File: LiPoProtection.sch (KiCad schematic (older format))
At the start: 51 parts, among them P1 CONN_01X05, P2 Load, P3 Supply, Q1 IRLML2502, U1 LM324, U2 LM324, U3 74HC08, U4 LP2950

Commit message: Added mass areas
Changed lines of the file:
@@
 $EndComp
 Wire Wire Line
-	6700 5350 6700 5950
-Wire Wire Line
-	6700 5950 6700 6700
+	6700 5350 6700 6700
 Wire Wire Line
 	8700 3725 9100 3725
@@
 	10100 3725 10000 3725
 Wire Wire Line
-	10000 3725 10000 3975
-Wire Wire Line
-	10000 3975 9700 3975
-Wire Wire Line
-	9700 3975 9400 3975
+	10000 3975 10000 3725
+Wire Wire Line
+	9400 3975 10000 3975
 Wire Wire Line
 	9400 3975 9400 3875
@@
 	2800 1050 3000 1050
 Wire Wire Line
-	2700 1550 2800 1550
-Wire Wire Line
-	2800 1550 2950 1550
+	2700 1550 2950 1550
 Wire Wire Line
 	2800 1350 2800 1550
@@
 	2100 1550 2400 1550
 Wire Wire Line
-	2100 1050 2100 1350
-Wire Wire Line
-	2100 1350 2100 1550
-Wire Wire Line
-	2100 1550 2100 2650
+	2100 1050 2100 2650
 Wire Wire Line
 	2000 1750 2400 1750
 Wire Wire Line
-	2000 1050 2000 1750
-Wire Wire Line
-	2000 1750 2000 7050
-Wire Wire Line
-	2700 1750 2800 1750
-Wire Wire Line
-	2800 1750 2950 1750
-Wire Wire Line
-	3950 1650 3950 2450
-Wire Wire Line
-	3950 2450 3950 2950
-Wire Wire Line
-	3500 2450 3600 2450
-Wire Wire Line
-	3600 2450 3950 2450
+	2000 1050 2000 7050
+Wire Wire Line
+	2700 1750 2950 1750
+Wire Wire Line
+	3950 1650 3950 2950
+Wire Wire Line
+	3500 2450 3950 2450
 Wire Wire Line
 	2800 2450 3200 2450
 Wire Wire Line
-	2800 1750 2800 2300
-Wire Wire Line
-	2800 2300 2800 2450
+	2800 1750 2800 2450
 Connection ~ 2800 1750
 Wire Wire Line
 	2550 1050 2300 1050
 Wire Wire Line
-	2550 600  2550 750
-Wire Wire Line
-	2550 750  2550 1050
-Wire Wire Line
-	2550 750  3350 750
-Wire Wire Line
-	3350 750  4575 750
-Wire Wire Line
-	4575 750  5400 750
-Wire Wire Line
-	5400 750  6350 750
-Wire Wire Line
-	6350 750  7600 750
+	2550 600  2550 1050
+Wire Wire Line
+	2550 750  7600 750
 Wire Wire Line
 	3350 750  3350 1250
@@
 	5400 2100 5400 2050
 Wire Wire Line
-	4750 1550 4850 1550
-Wire Wire Line
-	4850 1550 5000 1550
+	4750 1550 5000 1550
 Wire Wire Line
 	4850 1350 4850 1550
@@
 	4050 1750 4450 1750
 Wire Wire Line
-	4750 1750 4850 1750
-Wire Wire Line
-	4850 1750 5000 1750
-Wire Wire Line
-	6000 1650 6000 2450
-Wire Wire Line
-	6000 2450 6000 3100
-Wire Wire Line
-	5550 2450 5625 2450
-Wire Wire Line
-	5625 2450 6000 2450
+	4750 1750 5000 1750
+Wire Wire Line
+	6000 1650 6000 3100
+Wire Wire Line
+	5550 2450 6000 2450
 Wire Wire Line
 	4850 2450 5250 2450
 Wire Wire Line
-	4850 1750 4850 2300
-Wire Wire Line
-	4850 2300 4850 2450
+	4850 1750 4850 2450
 Connection ~ 4850 1750
 Wire Wire Line
@@
 	7600 2100 7600 2050
 Wire Wire Line
-	6950 1550 7050 1550
-Wire Wire Line
-	7050 1550 7200 1550
+	6950 1550 7200 1550
 Wire Wire Line
 	7050 1350 7050 1550
@@
 	6650 1750 6250 1750
 Wire Wire Line
-	6950 1750 7050 1750
-Wire Wire Line
-	7050 1750 7200 1750
-Wire Wire Line
-	8200 1650 8200 2450
-Wire Wire Line
-	8200 2450 8200 3250
-Wire Wire Line
-	7750 2450 8000 2450
-Wire Wire Line
-	8000 2450 8200 2450
+	6950 1750 7200 1750
+Wire Wire Line
+	8200 1650 8200 3250
+Wire Wire Line
+	7750 2450 8200 2450
 Wire Wire Line
 	7050 2450 7450 2450
 Wire Wire Line
-	7050 1750 7050 2325
-Wire Wire Line
-	7050 2325 7050 2450
+	7050 1750 7050 2450
 Connection ~ 7050 1750
 Wire Wire Line
@@
 	6250 2650 6250 1750
 Wire Wire Line
-	2200 1050 2200 1150
-Wire Wire Line
-	2200 1150 2200 1300
+	2200 1050 2200 1300
 Wire Wire Line
 	2200 1150 2650 1150
@@
 	2650 850  4150 850
 Wire Wire Line
-	4150 850  4150 1550
-Wire Wire Line
-	4150 1550 4150 2650
+	4150 850  4150 2650
 Connection ~ 4150 1550
 Wire Wire Line
@@
 Connection ~ 7600 750
 Wire Wire Line
-	4850 1050 4975 1050
-Wire Wire Line
-	4975 1050 5050 1050
+	4850 1050 5050 1050
 Wire Wire Line
 	7050 1050 7250 1050
@@
 	2000 7050 5550 7050
 Wire Wire Line
-	2300 1050 2300 1500
-Wire Wire Line
-	2300 1500 1725 1500
-Wire Wire Line
-	1725 1500 1150 1500
+	2300 1500 2300 1050
+Wire Wire Line
+	1150 1500 2300 1500
 Connection ~ 2300 1050
 Wire Wire Line
 	4100 6400 4100 6350
 Wire Wire Line
-	850  4250 875  4250
-Wire Wire Line
-	875  4250 1200 4250
-Wire Wire Line
-	1200 4250 1550 4250
+	850  4250 1550 4250
 Wire Wire Line
 	1150 1500 1150 1550
 Wire Wire Line
-	1150 1800 1150 2000
-Wire Wire Line
-	1150 2000 1150 2150
-Wire Wire Line
-	750  2000 1150 2000
-Wire Wire Line
-	1150 2000 1350 2000
+	1150 1800 1150 2150
+Wire Wire Line
+	750  2000 1350 2000
 Wire Wire Line
 	1350 2000 1350 4050
@@
 	1050 2750 1150 2750
 Wire Wire Line
-	1150 2550 1150 2750
-Wire Wire Line
-	1150 2750 1150 2850
-Wire Wire Line
-	750  2000 750  2350
-Wire Wire Line
-	750  2350 750  2750
+	1150 2550 1150 2850
+Wire Wire Line
+	750  2000 750  2750
 Wire Wire Line
 	750  2350 800  2350
@@
 	3700 6700 3950 6700
 Wire Wire Line
-	3700 6050 3700 6125
-Wire Wire Line
-	3700 6125 3700 6700
-Wire Wire Line
-	3500 6050 3550 6050
-Wire Wire Line
-	3550 6050 3700 6050
+	3700 6050 3700 6700
+Wire Wire Line
+	3500 6050 3700 6050
 Wire Wire Line
 	3550 6300 3550 6050
@@
 	5700 6700 5950 6700
 Wire Wire Line
-	5700 6050 5700 6125
-Wire Wire Line
-	5700 6125 5700 6700
-Wire Wire Line
-	5500 6050 5550 6050
-Wire Wire Line
-	5550 6050 5700 6050
+	5700 6050 5700 6700
+Wire Wire Line
+	5500 6050 5700 6050
 Wire Wire Line
 	5550 6300 5550 6050
@@
 	3700 5050 3950 5050
 Wire Wire Line
-	3700 4400 3700 4500
-Wire Wire Line
-	3700 4500 3700 5050
-Wire Wire Line
-	3500 4400 3550 4400
-Wire Wire Line
-	3550 4400 3700 4400
+	3700 4400 3700 5050
+Wire Wire Line
+	3500 4400 3700 4400
 Wire Wire Line
 	3550 4650 3550 4400
@@
 	5700 4950 5950 4950
 Wire Wire Line
-	5700 4300 5700 4375
-Wire Wire Line
-	5700 4375 5700 4950
-Wire Wire Line
-	5500 4300 5550 4300
-Wire Wire Line
-	5550 4300 5700 4300
+	5700 4300 5700 4950
+Wire Wire Line
+	5500 4300 5700 4300
 Wire Wire Line
 	5550 4550 5550 4300
@@
 	4700 6700 4250 6700
 Wire Wire Line
-	4700 5250 4700 5950
-Wire Wire Line
-	4700 5950 4700 6700
+	4700 5250 4700 6700
 Connection ~ 6700 5950
 Wire Wire Line
-	6700 4200 6700 4950
-Wire Wire Line
-	6700 4950 6700 5050
+	6700 4200 6700 5050
 Connection ~ 6700 4950
 Wire Wire Line
@@
 	4950 4850 4950 3250
 Wire Wire Line
-	4700 4300 4700 5050
-Wire Wire Line
-	4700 5050 4700 5150
+	4700 4300 4700 5150
 Connection ~ 4700 5050
 Connection ~ 4700 5950
@@
 	2950 4950 2950 3100
 Wire Wire Line
-	7650 3800 7650 4000
-Wire Wire Line
-	7650 4000 7650 4100
+	7650 3800 7650 4100
 Connection ~ 7650 4000
 Wire Wire Line
@@
 	1050 4775 1050 4625
 Wire Wire Line
-	875  4625 1050 4625
-Wire Wire Line
-	1050 4625 1200 4625
+	875  4625 1200 4625
 Connection ~ 1050 4625
 Wire Wire Line
@@
 	8700 4450 8700 3725
 Wire Wire Line
-	1050 600  1350 600
-Wire Wire Line
-	1350 600  2550 600
+	1050 600  2550 600
 Wire Wire Line
 	7950 4000 7650 4000
 Wire Wire Line
-	1725 1500 1725 5525
-Wire Wire Line
-	1725 5525 1725 5750
+	1725 1500 1725 5750
 Connection ~ 1725 1500
 Wire Wire Line
@@
 	1725 6050 1050 6050
 Wire Wire Line
-	1050 6050 1050 5900
-Wire Wire Line
-	1050 5900 925  5900
-Wire Wire Line
-	925  5900 900  5900
+	1050 5900 1050 6050
+Wire Wire Line
+	900  5900 1050 5900
 Wire Wire Line
 	925  5625 925  5900
@@
 	875  5425 925  5425
 Wire Wire Line
-	4700 5250 7100 5250
-Wire Wire Line
-	7100 5250 7525 5250
+	4700 5250 7525 5250
 Wire Wire Line
 	7525 5250 7525 5050
@@
 	7775 5150 7775 5250
 Wire Wire Line
-	6700 5050 7200 5050
-Wire Wire Line
-	7200 5050 7225 5050
+	6700 5050 7225 5050
 Wire Wire Line
 	7225 5050 7225 5750

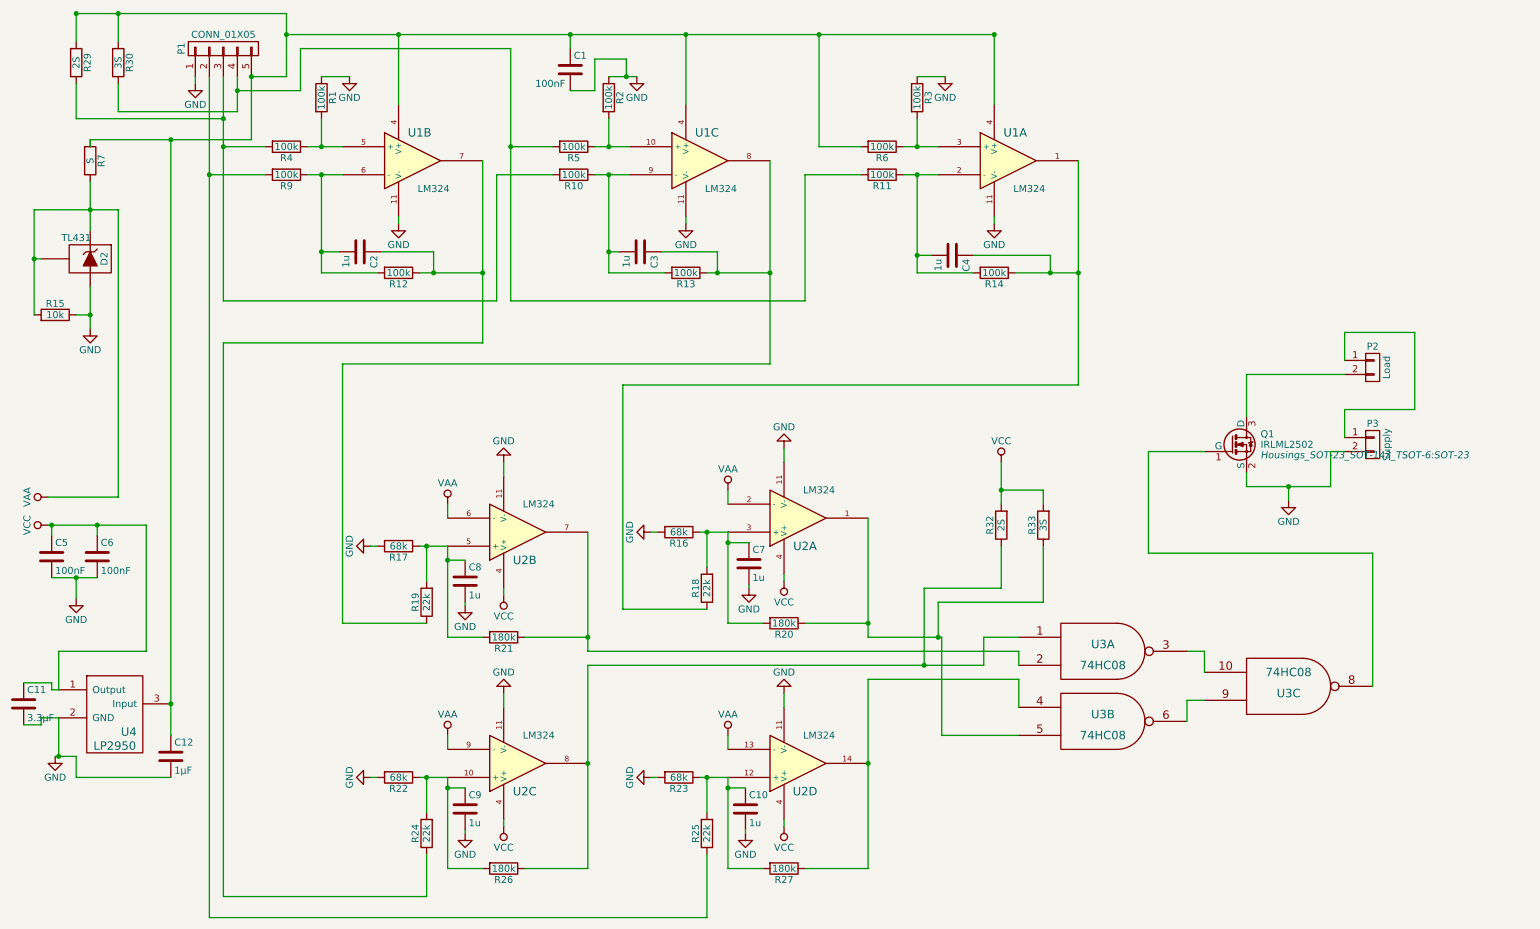
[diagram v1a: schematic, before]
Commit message: Added libraries, added flyout diode
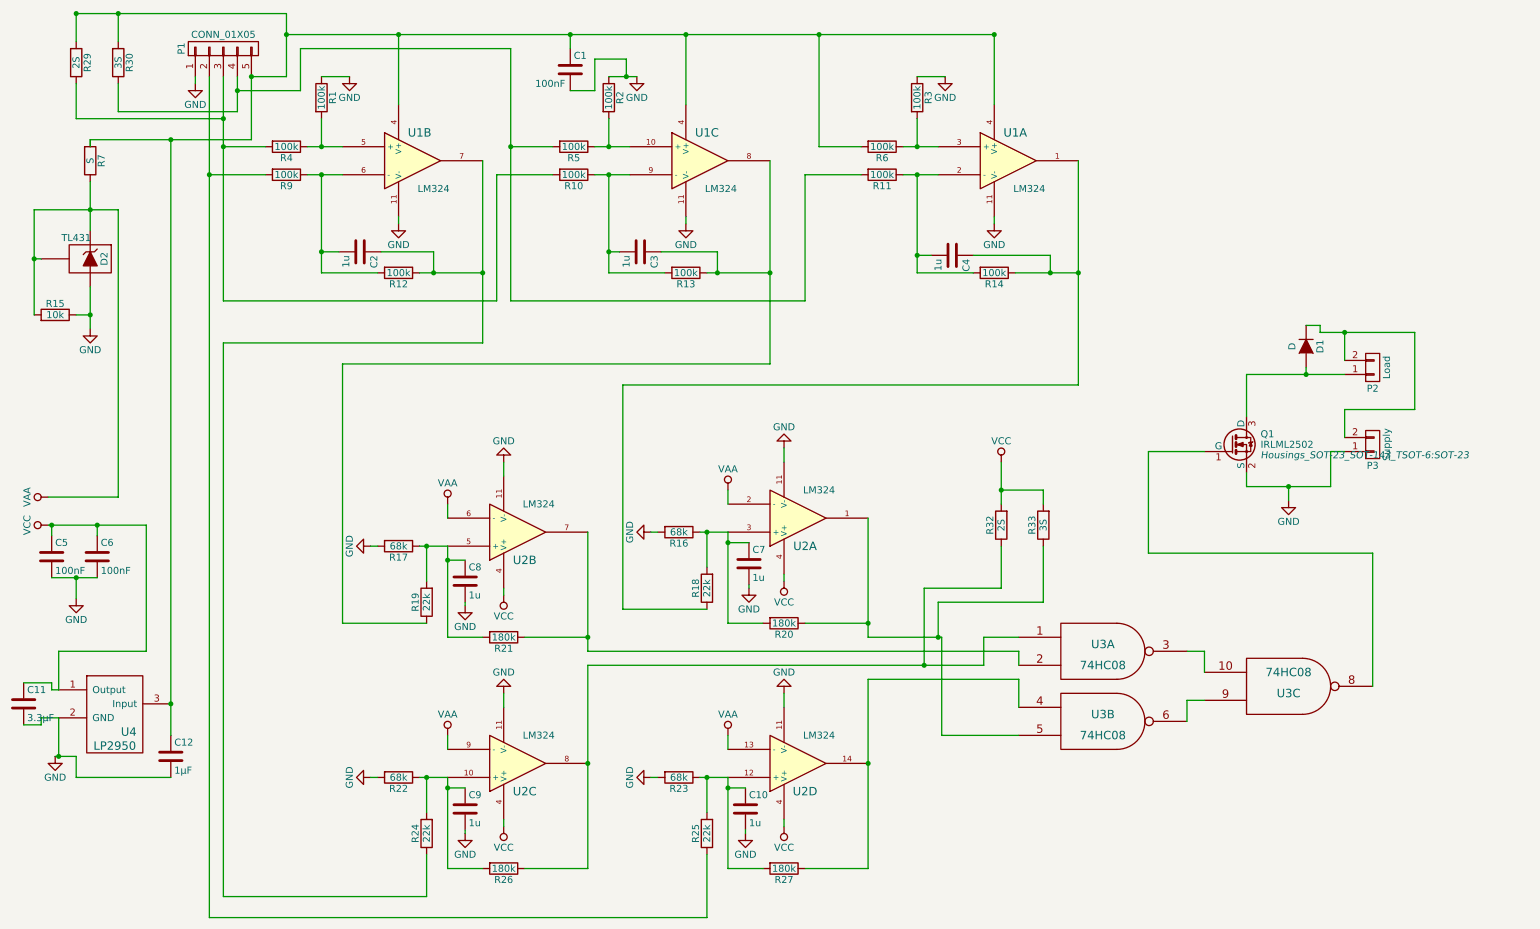
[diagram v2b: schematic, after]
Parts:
- added D1: D, Diodes_ThroughHole:Diode_DO-41_SOD81_Horizontal_RM10, symbol D
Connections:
- net GND: now also P3.1 (P1); no longer P3.2 (P2)
- net at Q1.3 (D): now also P2.1 (P1), D1.2 (A); no longer P2.2 (P2)
- new net: D1.1 (K), P2.2 (P2), P3.2 (P2)
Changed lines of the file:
@@
 LIBS:contrib
 LIBS:valves
-LIBS:cmos4000ex
+LIBS:74xx_ex
+LIBS:device_ex
+LIBS:regul_ex
 LIBS:transistors_ex
-LIBS:device_ex
-LIBS:74xx_ex
-LIBS:regul_ex
+LIBS:cmos4000_ex
 LIBS:LiPoProtection-cache
 EELAYER 25 0
@@
 F 3 "" H 10300 3675 60  0000 C CNN
 	1    10300 3675
-	1    0    0    -1
+	1    0    0    1
 $EndComp
 $Comp
@@
 F 3 "" H 10300 3125 60  0000 C CNN
 	1    10300 3125
-	1    0    0    -1
+	1    0    0    1
 $EndComp
 $Comp
@@
 	10100 3075 10100 2875
 Wire Wire Line
-	10100 2875 10600 2875
+	9925 2875 10600 2875
 Wire Wire Line
 	10600 2875 10600 3425
@@
 	10100 3725 10000 3725
 Wire Wire Line
-	10000 3975 10000 3725
-Wire Wire Line
-	9400 3975 10000 3975
+	10000 3725 10000 3975
+Wire Wire Line
+	10000 3975 9400 3975
 Wire Wire Line
 	9400 3975 9400 3875
@@
 	2000 7050 5550 7050
 Wire Wire Line
-	2300 1500 2300 1050
-Wire Wire Line
-	1150 1500 2300 1500
+	2300 1050 2300 1500
+Wire Wire Line
+	2300 1500 1150 1500
 Connection ~ 2300 1050
 Wire Wire Line
@@
 	1725 6050 1050 6050
 Wire Wire Line
-	1050 5900 1050 6050
-Wire Wire Line
-	900  5900 1050 5900
+	1050 6050 1050 5900
+Wire Wire Line
+	1050 5900 900  5900
 Wire Wire Line
 	925  5625 925  5900
@@
 	7100 4700 7100 5250
 Connection ~ 7100 5250
+$Comp
+L D D1
+U 1 1 55F855C6
+P 9825 2975
+F 0 "D1" H 9825 3075 50  0000 C CNN
+F 1 "D" H 9825 2875 50  0000 C CNN
+F 2 "Diodes_ThroughHole:Diode_DO-41_SOD81_Horizontal_RM10" H 9825 2975 60  0001 C CNN
+F 3 "" H 9825 2975 60  0000 C CNN
+	1    9825 2975
+	0    1    1    0
+$EndComp
+Wire Wire Line
+	9925 2875 9925 2825
+Wire Wire Line
+	9925 2825 9825 2825
+Connection ~ 10100 2875
+Wire Wire Line
+	9825 3125 9825 3175
+Connection ~ 9825 3175
 $EndSCHEMATC
